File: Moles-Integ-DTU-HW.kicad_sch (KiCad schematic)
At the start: 78 parts, among them J1 PWR, J2 USB_B_Mini, J3 DISP, J4 PROG, J5 RF_MOD, Q2 MMSS8050-H-TP, SW1 BOOT, SW2 EN, U1 AZ1117-3.3, U2 ESP32-WROOM-32D, U3 nRF24L01P

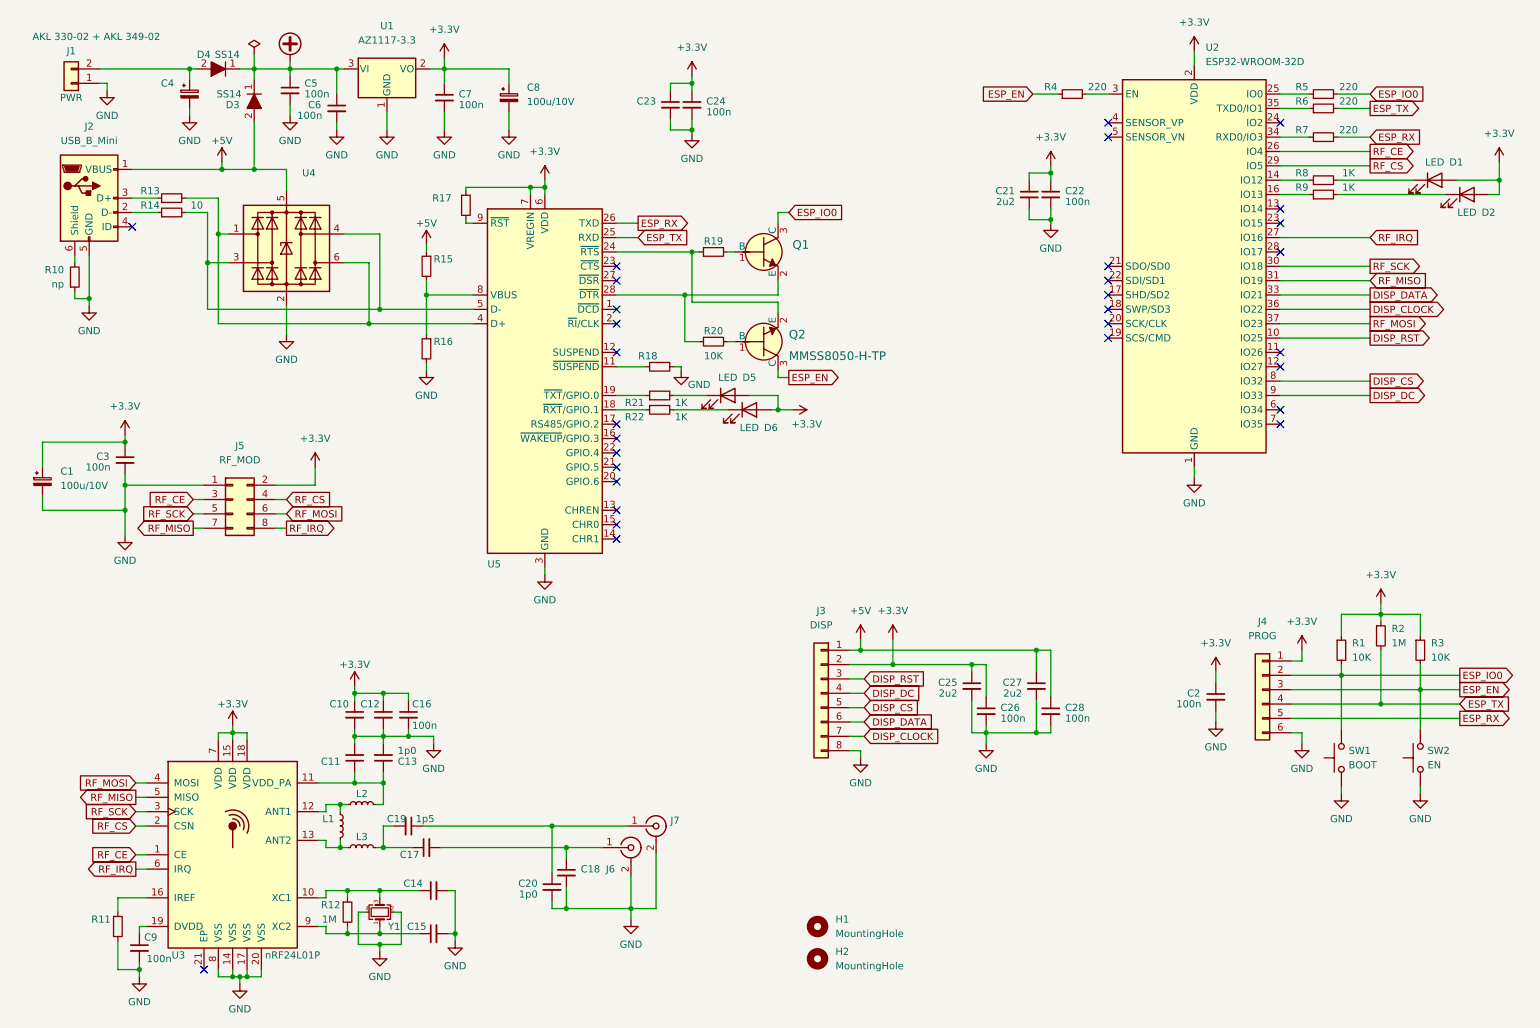
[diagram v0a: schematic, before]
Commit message: Added Text to PCB silkscreen and updated 3D
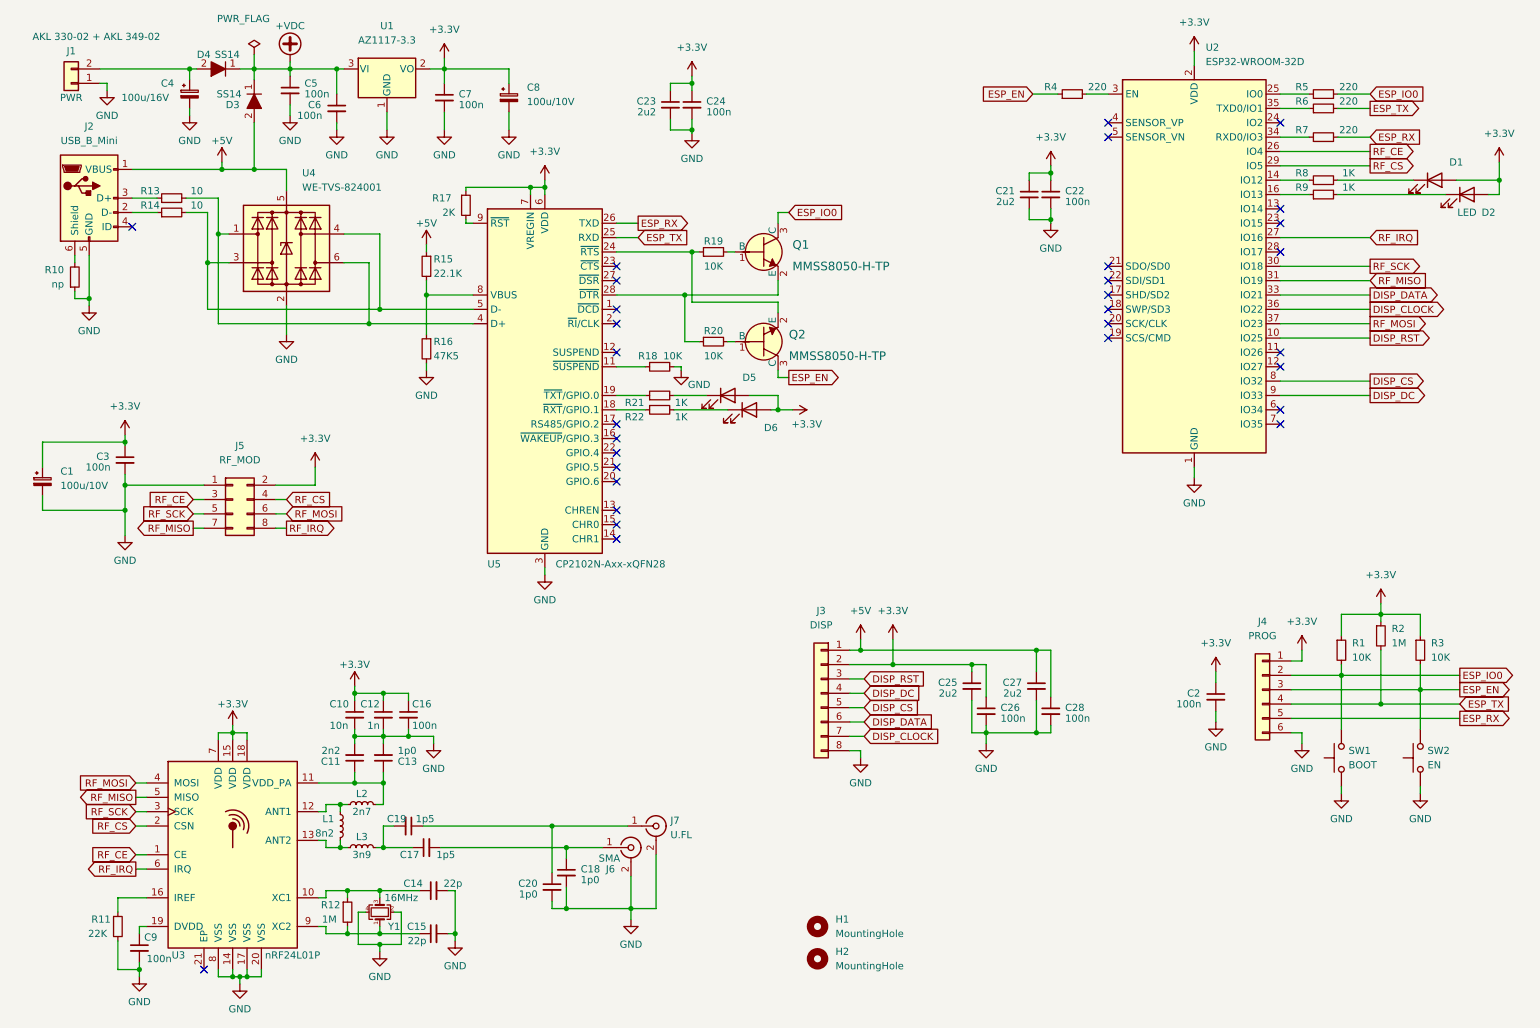
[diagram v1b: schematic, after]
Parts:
- C10: value (none) -> 10n; footprint (none) -> Capacitor_SMD:C_0603_1608Metric_Pad1.08x0.95mm_HandSolder
- C11: value (none) -> 2n2; footprint (none) -> Capacitor_SMD:C_0402_1005Metric_Pad0.74x0.62mm_HandSolder
- C12: value (none) -> 1n; footprint (none) -> Capacitor_SMD:C_0603_1608Metric_Pad1.08x0.95mm_HandSolder
- C14, C15: value (none) -> 22p; footprint (none) -> Capacitor_SMD:C_0402_1005Metric_Pad0.74x0.62mm_HandSolder
- C17: value (none) -> 1p5; footprint (none) -> Capacitor_SMD:C_0402_1005Metric_Pad0.74x0.62mm_HandSolder
- C18: value (none) -> 1p0; footprint (none) -> Capacitor_SMD:C_0402_1005Metric_Pad0.74x0.62mm_HandSolder
- C23: value (none) -> 2u2; footprint (none) -> Capacitor_SMD:C_0603_1608Metric_Pad1.08x0.95mm_HandSolder
- C4: value (none) -> 100u/16V; footprint (none) -> Capacitor_THT:C_Radial_D6.3mm_H11.0mm_P2.50mm
- D1, D5, D6: value LED -> (none); footprint LED_SMD:LED_0603_1608Metric_Pad1.05x0.95mm_HandSolder -> (none)
- J6: value (none) -> SMA; footprint (none) -> Connector_Coaxial:SMA_Amphenol_901-143_Horizontal
- J7: value (none) -> U.FL; footprint (none) -> Connector_Coaxial:U.FL_Hirose_U.FL-R-SMT-1_Vertical
- L1: value (none) -> 8n2; footprint (none) -> Inductor_SMD:L_0402_1005Metric_Pad0.77x0.64mm_HandSolder
- L2: value (none) -> 2n7; footprint (none) -> Inductor_SMD:L_0402_1005Metric_Pad0.77x0.64mm_HandSolder
- L3: value (none) -> 3n9; footprint (none) -> Inductor_SMD:L_0402_1005Metric_Pad0.77x0.64mm_HandSolder
- Q1: value (none) -> MMSS8050-H-TP; footprint (none) -> Package_TO_SOT_SMD:SOT-23
- Q2: footprint (none) -> Package_TO_SOT_SMD:SOT-23
- R11: value (none) -> 22K; footprint (none) -> Resistor_SMD:R_0603_1608Metric_Pad0.98x0.95mm_HandSolder
- R13: value (none) -> 10; footprint (none) -> Resistor_SMD:R_0603_1608Metric_Pad0.98x0.95mm_HandSolder
- R15: value (none) -> 22.1K; footprint (none) -> Resistor_SMD:R_0603_1608Metric_Pad0.98x0.95mm_HandSolder
- R16: value (none) -> 47K5; footprint (none) -> Resistor_SMD:R_0603_1608Metric_Pad0.98x0.95mm_HandSolder
- R17: value (none) -> 2K; footprint (none) -> Resistor_SMD:R_0603_1608Metric_Pad0.98x0.95mm_HandSolder
- R18, R19: value (none) -> 10K; footprint (none) -> Resistor_SMD:R_0603_1608Metric_Pad0.98x0.95mm_HandSolder
- U4: value (none) -> WE-TVS-824001; footprint (none) -> Package_TO_SOT_SMD:SOT-23-6
- U5: value (none) -> CP2102N-Axx-xQFN28; footprint (none) -> Package_DFN_QFN:QFN-28-1EP_5x5mm_P0.5mm_EP3.35x3.35mm
- Y1: value (none) -> 16MHz; footprint (none) -> Crystal:Crystal_SMD_3225-4Pin_3.2x2.5mm_HandSoldering
